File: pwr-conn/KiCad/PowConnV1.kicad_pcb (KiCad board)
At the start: 2 copper layers, 17.3 x 21.5 mm, 5 parts, among them P1 8Pin_2x4_inline, P2 PAD, P3 PAD, P4 PAD, P5 PAD

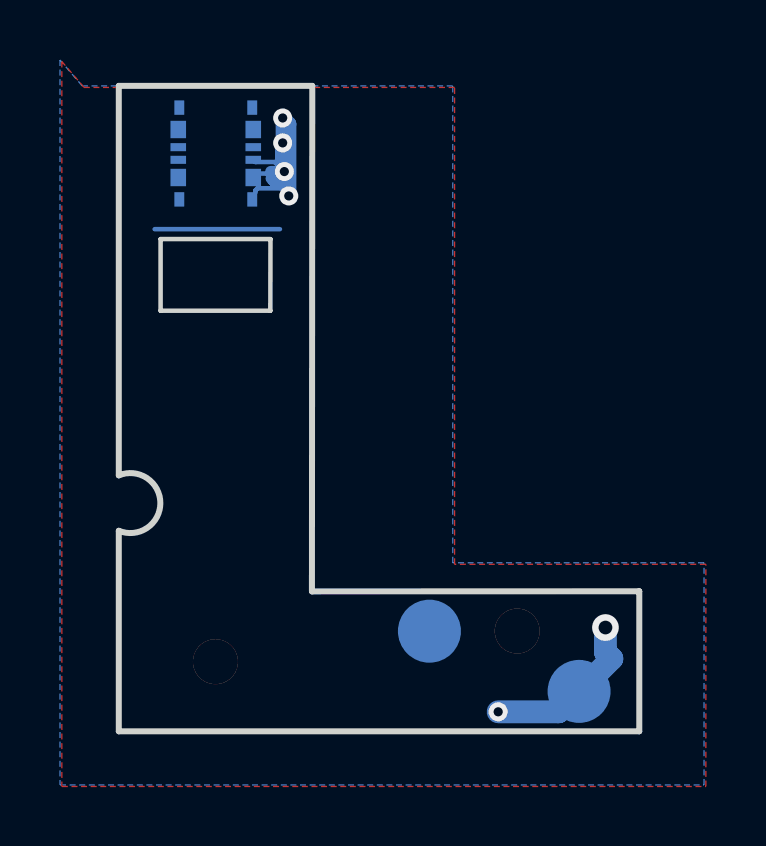
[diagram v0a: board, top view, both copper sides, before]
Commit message: As described in JIRA EL-160
1. Shift the cutout on the side
2. Add bigger no-copper space around holes to avoid contact with screw heads
3. Widen the part with contacts by 1mm
4. Rename to G935F-PWR
5. Label with sensorable.io and the date in yyyy-mm-dd format.
6. Leave all contacts and footprints exactly where they are.
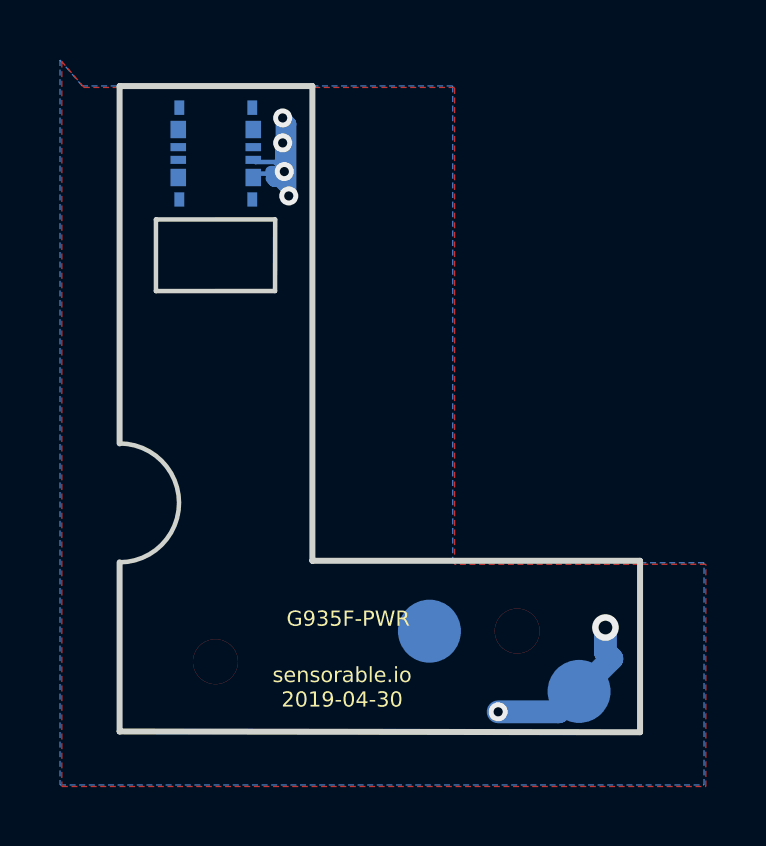
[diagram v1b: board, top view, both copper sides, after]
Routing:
- net GND1: track 4.18 -> 0.00 mm
- net Dev+: track 21.1 -> 20.1 mm
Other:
- outline, holes or cut-outs redrawn
- board text added: "G935F-PWR"
- board text added: "sensorable.io 2019-04-30"
- board text removed: "PowConnV1"
- board text removed: "sensorable.io DEC2018"
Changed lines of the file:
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@@
-(kicad_pcb (version 20171130) (host pcbnew "(5.0.1)-4")
+(kicad_pcb (version 20171130) (host pcbnew "(5.0.2)-1")
   (general
     (thickness 1.6)
-    (drawings 74)
-    (tracks 46)
+    (drawings 94)
+    (tracks 42)
     (zones 0)
     (modules 5)
     (nets 3)
   )
-  (page A4)
+  (page A)
   (title_block
-    (title S7Traf_PowConn)
-    (date 2018-12-04)
-    (rev V1)
+    (title G935F-PWR)
+    (date 2019-04-27)
+    (rev V2)
     (company "Roman Dasovic")
   )
@@
     (45 Margin user)
     (46 B.CrtYd user)
-    (47 F.CrtYd user hide)
+    (47 F.CrtYd user)
     (48 B.Fab user)
-    (49 F.Fab user hide)
+    (49 F.Fab user)
   )
   (setup
@@
     (mod_text_size 1 1)
     (mod_text_width 0.15)
-    (pad_size 2.1 2.1)
-    (pad_drill 0)
+    (pad_size 1.5 1.5)
+    (pad_drill 1.5)
     (pad_to_mask_clearance 0)
     (solder_mask_min_width 0.1016)
@@
       (effects (font (size 0.127 0.127) (thickness 0.03175)))
     )
-    (pad "" thru_hole circle (at 0 0) (size 1.5 1.5) (drill 1.5) (layers *.Cu *.Mask))
+    (pad "" thru_hole circle (at 0 0) (size 1.5 1.5) (drill 1.5) (layers *.Cu *.Mask)
+      (clearance 1.016))
   )
   (module Footprints:NPTH_1.5mm (layer F.Cu)
@@
       (effects (font (size 0.127 0.127) (thickness 0.03175)))
     )
-    (pad "" thru_hole circle (at 0 0) (size 1.5 1.5) (drill 1.5) (layers *.Cu *.Mask))
+    (pad "" thru_hole circle (at 0 0) (size 1.5 1.5) (drill 1.5) (layers *.Cu *.Mask)
+      (clearance 1.016))
   )
   (module Footprints:PAD_2.1mm_circle (layer B.Cu)
@@
       (net 1 GND1) (zone_connect 2))
   )
-  (gr_text PowConnV1 (at 114.30762 84.18068) (layer B.SilkS)
+  (gr_arc (start 110.9472 89.7636) (end 110.9472 91.7448) (angle -180) (layer Edge.Cuts) (width 0.15))
+  (gr_circle (center 114.1546 95.03162) (end 115.6546 95.03162) (layer Margin) (width 0.1))
+  (gr_line (start -290.266377 297.197305) (end -288.266377 297.197305) (layer Margin) (width 0.1))
+  (gr_line (start 110.9296 75.850798) (end 110.9296 87.760844) (layer Margin) (width 0.1))
+  (gr_line (start 117.3796 75.850798) (end 110.9296 75.850798) (layer Margin) (width 0.1))
+  (gr_arc (start 110.814834 89.757549) (end 112.814834 89.757549) (angle -86.71040722) (layer Margin) (width 0.1))
+  (gr_line (start 117.3796 91.697543) (end 117.3796 75.850798) (layer Margin) (width 0.1))
+  (gr_line (start 117.3796 91.697543) (end 128.279324 91.697543) (layer Margin) (width 0.1))
+  (gr_line (start 128.279324 91.697543) (end 128.279324 97.365698) (layer Margin) (width 0.1))
+  (gr_circle (center 124.21254 94.03162) (end 125.71254 94.03162) (layer Margin) (width 0.1))
+  (gr_line (start 110.9296 97.365698) (end 128.279324 97.365698) (layer Margin) (width 0.1))
+  (gr_line (start 110.9296 91.754253) (end 110.9296 97.365698) (layer Margin) (width 0.1))
+  (gr_arc (start 110.814834 89.757549) (end 110.9296 91.754253) (angle -86.71040722) (layer Margin) (width 0.1))
+  (gr_circle (center 114.1546 95.03162) (end 114.9046 95.03162) (layer Margin) (width 0.1))
+  (gr_circle (center 124.21254 94.03162) (end 124.96254 94.03162) (layer Margin) (width 0.1))
+  (gr_line (start 112.1296 80.3148) (end 116.1796 80.3148) (layer Margin) (width 0.1))
+  (gr_line (start 112.1296 82.671301) (end 112.1296 80.3148) (layer Margin) (width 0.1))
+  (gr_line (start 116.1796 82.671301) (end 112.1296 82.671301) (layer Margin) (width 0.1))
+  (gr_line (start 116.1796 80.3148) (end 116.1796 82.671301) (layer Margin) (width 0.1))
+  (gr_text "sensorable.io\n2019-04-30" (at 118.364 95.9104) (layer F.SilkS)
+    (effects (font (size 0.508 0.508) (thickness 0.127)))
+  )
+  (gr_text G935F-PWR (at 118.5672 93.6244) (layer F.SilkS)
+    (effects (font (size 0.508 0.508) (thickness 0.127)))
+  )
+  (gr_line (start 116.1288 80.3148) (end 112.15812 80.31612) (layer Edge.Cuts) (width 0.15))
+  (gr_line (start 116.1288 82.7024) (end 116.13388 80.31988) (layer Edge.Cuts) (width 0.15))
+  (gr_line (start 112.15812 82.70372) (end 116.1288 82.7024) (layer Edge.Cuts) (width 0.15))
+  (gr_line (start 112.15812 80.31612) (end 112.15812 82.70372) (layer Edge.Cuts) (width 0.15))
+  (gr_text G935F-PWR (at 114.30762 84.18068) (layer B.SilkS)
     (effects (font (size 0.508 0.508) (thickness 0.127)) (justify mirror))
   )
-  (gr_text "sensorable.io\nDEC2018" (at 114.33048 86.47938) (layer B.SilkS)
+  (gr_text "sensorable.io\n2019-04-30" (at 114.4016 86.3092) (layer B.SilkS)
     (effects (font (size 0.508 0.508) (thickness 0.127)) (justify mirror))
   )
   (gr_line (start 115.75034 79.43342) (end 115.93322 79.43088) (layer B.SilkS) (width 0.2))
-  (gr_line (start 116.17452 80.81264) (end 115.9383 80.57642) (layer B.SilkS) (width 0.2))
-  (gr_line (start 115.9383 78.80604) (end 115.9383 80.57642) (layer B.SilkS) (width 0.2))
+  (gr_line (start 116.7384 80.8228) (end 115.9256 80.01) (layer B.SilkS) (width 0.2))
+  (gr_line (start 115.9383 78.80604) (end 115.9256 80.01) (layer B.SilkS) (width 0.2))
   (gr_line (start 115.74526 78.80604) (end 115.9383 78.80604) (layer B.SilkS) (width 0.2))
   (gr_line (start 112.00638 78.40472) (end 112.00892 78.40726) (layer B.SilkS) (width 0.2))
@@
     (effects (font (size 0.508 0.508) (thickness 0.127)) (justify mirror))
   )
-  (gr_text DEV+ (at 116.46916 81.96834 90) (layer B.SilkS)
+  (gr_text DEV+ (at 116.7892 81.96834 90) (layer B.SilkS)
     (effects (font (size 0.508 0.508) (thickness 0.127)) (justify mirror))
   )
@@
   (gr_circle (center 126.25832 96.07296) (end 125.80112 94.96298) (layer B.SilkS) (width 0.2))
   (gr_circle (center 121.29262 94.0562) (end 122.04192 93.06306) (layer B.SilkS) (width 0.2))
-  (gr_line (start 115.97132 83.35772) (end 115.9764 80.9752) (layer Edge.Cuts) (width 0.15))
-  (gr_line (start 112.31372 83.35772) (end 115.97132 83.35772) (layer Edge.Cuts) (width 0.15))
-  (gr_line (start 112.31372 80.97012) (end 112.31372 83.35772) (layer Edge.Cuts) (width 0.15))
-  (gr_line (start 115.9764 80.97012) (end 112.31372 80.97012) (layer Edge.Cuts) (width 0.15))
-  (gr_line (start 110.920275 75.863255) (end 117.370275 75.863255) (layer Edge.Cuts) (width 0.2))
-  (gr_line (start 110.920275 97.378154) (end 128.27 97.378154) (layer Edge.Cuts) (width 0.2))
-  (gr_arc (start 111.30551 89.770005) (end 110.920275 90.692824) (angle -225.3166138) (layer Edge.Cuts) (width 0.2))
-  (gr_line (start 128.27 97.378154) (end 128.27 92.71) (layer Edge.Cuts) (width 0.2))
-  (gr_line (start 110.920275 90.692824) (end 110.920275 97.378154) (layer Edge.Cuts) (width 0.2))
-  (gr_line (start 117.35816 92.71508) (end 117.370275 75.863255) (layer Edge.Cuts) (width 0.2))
-  (gr_line (start 110.920275 75.863255) (end 110.920275 88.847187) (layer Edge.Cuts) (width 0.2))
-  (gr_line (start 128.27 92.71) (end 117.35816 92.71508) (layer Edge.Cuts) (width 0.2))
+  (gr_line (start 110.9472 75.8698) (end 117.3734 75.8698) (layer Edge.Cuts) (width 0.2))
+  (gr_line (start 110.9472 97.3836) (end 128.2954 97.409) (layer Edge.Cuts) (width 0.2))
+  (gr_line (start 128.2954 97.409) (end 128.2954 91.694) (layer Edge.Cuts) (width 0.2))
+  (gr_line (start 110.9472 91.7448) (end 110.9472 97.3836) (layer Edge.Cuts) (width 0.2))
+  (gr_line (start 117.3734 91.694) (end 117.3734 75.8698) (layer Edge.Cuts) (width 0.2))
+  (gr_line (start 110.9472 75.8698) (end 110.9472 87.7824) (layer Edge.Cuts) (width 0.2))
+  (gr_line (start 128.2954 91.694) (end 117.3734 91.694) (layer Edge.Cuts) (width 0.2))
   (gr_line (start 128.296925 92.695176) (end 117.3972 92.695176) (layer Eco1.User) (width 0.2))
   (gr_line (start 110.9472 76.348431) (end 117.3972 76.348431) (layer Eco1.User) (width 0.2))
@@
   (gr_line (start 128.296925 97.36333) (end 128.296925 92.695176) (layer Eco1.User) (width 0.2))
   (gr_line (start 110.9472 90.678) (end 110.9472 97.36333) (layer Eco1.User) (width 0.2))
-  (segment (start 112.1156 80.63992) (end 116.29136 80.63992) (width 0.1524) (layer B.Cu) (net 1))
   (via (at 127.14224 93.91904) (size 0.889) (drill 0.4572) (layers F.Cu B.Cu) (net 2))
   (segment (start 127.313399 94.090199) (end 127.14224 93.91904) (width 0.1524) (layer B.Cu) (net 2))
@@
   (segment (start 116.22532 78.45552) (end 116.22532 78.19644) (width 0.1524) (layer B.Cu) (net 2))
   (segment (start 115.89512 78.78572) (end 115.89512 78.8416) (width 0.1524) (layer B.Cu) (net 2))
-  (segment (start 115.47857 79.34219) (end 115.47857 79.41808) (width 0.1524) (layer B.Cu) (net 2))
-  (segment (start 115.54228 79.27848) (end 115.47857 79.34219) (width 0.1524) (layer B.Cu) (net 2))
-  (segment (start 116.332 79.27848) (end 115.54228 79.27848) (width 0.1524) (layer B.Cu) (net 2))
   (segment (start 116.332 79.27848) (end 116.586 79.53248) (width 0.1524) (layer B.Cu) (net 2))
   (via (at 116.586 79.53248) (size 0.635) (drill 0.3048) (layers F.Cu B.Cu) (net 2))
@@
     )
   )
-  (zone (net 0) (net_name "") (layer B.Cu) (hatch edge 0.508)
-    (connect_pads (clearance 0.2032))
-    (min_thickness 0.1524)
-    (keepout (tracks not_allowed) (vias not_allowed) (copperpour not_allowed))
-    (fill (arc_segments 16) (thermal_gap 0.254) (thermal_bridge_width 0.2032))
-    (polygon
-      (pts
-        (xy 113.05032 77.37348) (xy 113.05032 79.85252) (xy 115.24996 79.85252) (xy 115.24996 77.43444) (xy 113.15192 77.43444)
-      )
-    )
-  )
   (zone (net 2) (net_name Dev+) (layer F.Cu) (hatch edge 0.508)
     (connect_pads (clearance 0.2032))
@@
       )
     )
+  )
+  (zone (net 0) (net_name "") (layer B.Cu) (hatch edge 0.508)
+    (connect_pads (clearance 0.2032))
+    (min_thickness 0.1524)
+    (keepout (tracks not_allowed) (vias not_allowed) (copperpour not_allowed))
+    (fill (arc_segments 16) (thermal_gap 0.254) (thermal_bridge_width 0.2032))
+    (polygon
+      (pts
+        (xy 113.1316 80.0608) (xy 115.2144 80.0608) (xy 115.19662 76.0984) (xy 113.09858 76.0984)
+      )
+    )

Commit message: kicad files, ready for assembly
as processed for the mfg+assembly .zip
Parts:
- moved P1 76.1 mm to (40.3, 96.4)
- moved P2 76.1 mm to (40.3, 113.4)
- moved P3 76.1 mm to (50.3, 112.3)
- moved P4 76.1 mm to (52.4, 114.4)
- moved P5 76.1 mm to (47.4, 112.4)
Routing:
- net Dev+: track 20.1 -> 21.0 mm
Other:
- board text added: "Assembly Instructions:"
- board text added: "Copper Layers: 2 Soldermask Layers: 2 Silkscreen Layers: 2 All Layers: Trace Width / Trace Spacing : 6/6 mil Outer Layers: 1 oz copper Inner Layers: .5 oz copper Minimum Via Annular Ring / Drill Diameter: 25mil / 12mil Dielectric: FR-4 Finished board thickness: 1.0mm +- 10%"
- board text added: "Direction of Unreeling"
- board text added: "FILE DESCRIPTIONS:"
- board text added: "Figure 1"
- board text added: "Front Face Orientation"
- board text added: "Orientation 0 degrees"
- board text added: "Orientation 180 degrees"
- board text added: "Orientation 270 degrees"
- board text added: "Orientation 90 degrees"
- board text added: "PCB Manufacturing Requirements:"
- board text added: "Please ask for clarification if any instructions are unclear. Assembly Instructions: 1. The .POS file contains centroid X-Y data and orientation. Orientation is such that 0 degrees indicates placement as if the reel sprocket holes are NORTH of the component. Refer to Figure 1. Do not place any items labeled as DNU. 2. BOM.csv containts BOM, quantities, and part numbers. Please advise before makin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"
- board text added: "Reel"
- board text added: "Round Sprocket Holes"
- board text added: "~~~~~~~~~~~~~~~~~~~~~~~~~~~~~~~~~~~~~~~~~~~~~~~~~~~~~~~~~~~~~~~~~~~~~~~~~~~~~~~~~~~~~~~~~~~~~~~~~~~~~~~~~~~~~~~~~~~~~~~~~~~~~~~~~~~~~~~~~~~~~~~~~~~~~~~~~~~~~~~~~~~~~~ ~~~~~~~~~~~~~~~~~~~~~~~~~~~~~~~~~~~~~~~~~~~~~~~~~~~~~~~~~~~~~~~~~~~~~~~~~~~~~~~~~~~~~~~~~~~~~~~~~~~~~~~~~~~~~~~~~~~~~~~~~~~~~~~~~~~~~~~~~~~~~~~~~~~~~~~~~~~~~~~~~~~~~~ Manufacturing Gerber Files -- Files needed for PCB Manufacturing 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"

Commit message: updated date/version
change to may 3 2019
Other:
- board text added: "sensorable.io 2019-05-03"
- board text removed: "sensorable.io 2019-04-30"
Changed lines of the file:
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@@
     (visible_elements 7FFFFFFF)
     (pcbplotparams
-      (layerselection 0x311fc_ffffffff)
+      (layerselection 0x00030_7ffffffe)
       (usegerberextensions true)
       (usegerberattributes false)
@@
       (padsonsilk false)
       (subtractmaskfromsilk false)
-      (outputformat 1)
+      (outputformat 4)
       (mirror false)
       (drillshape 0)
@@
   (module Footprints:8pin_molex_s7BatteryConn_5050040810 (layer B.Cu)
     (at 40.28948 96.43148)
+    (attr smd)
     (fp_text reference P1 (at -2.23012 -1.38684 90) (layer B.SilkS)
       (effects (font (size 0.3 0.3) (thickness 0.075)) (justify mirror))
@@
   (module Footprints:PAD_2.1mm_circle (layer B.Cu)
     (at 52.4002 114.36096)
+    (attr smd)
     (fp_text reference P4 (at 1.59258 0.14732) (layer B.SilkS)
       (effects (font (size 0.3 0.15) (thickness 0.03175)) (justify mirror))
@@
   (module Footprints:PAD_2.1mm_circle (layer B.Cu)
     (at 47.41164 112.35436)
+    (attr smd)
     (fp_text reference P5 (at 1.32588 1.04394) (layer B.SilkS)
       (effects (font (size 0.3 0.15) (thickness 0.03175)) (justify mirror))
@@
   (gr_line (start 42.3164 100.984701) (end 38.2664 100.984701) (layer Margin) (width 0.1))
   (gr_line (start 42.3164 98.6282) (end 42.3164 100.984701) (layer Margin) (width 0.1))
-  (gr_text "sensorable.io\n2019-04-30" (at 44.5008 114.2238) (layer F.SilkS)
+  (gr_text "sensorable.io\n2019-05-03" (at 44.5008 114.2238) (layer F.SilkS)
     (effects (font (size 0.508 0.508) (thickness 0.127)))
   )
@@
     (effects (font (size 0.508 0.508) (thickness 0.127)) (justify mirror))
   )
-  (gr_text "sensorable.io\n2019-04-30" (at 40.5384 104.6226) (layer B.SilkS)
+  (gr_text "sensorable.io\n2019-05-03" (at 40.5384 104.6226) (layer B.SilkS)
     (effects (font (size 0.508 0.508) (thickness 0.127)) (justify mirror))
   )
